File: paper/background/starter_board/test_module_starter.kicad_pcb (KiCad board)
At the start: 2 copper layers, 140.6 x 82 mm, 15 parts, among them J1 Barrel_Jack_12V, J2 RS232_2CH_Module, M1 ERM_Motor, M2 Stepper_4wire, M3 Servo_3pin, U1 D24V22F5_Buck, U2 Pi_Pico_W, U3 DRV2605L_Breakout, U4 DRV8871_Breakout, U5 Tic_T500

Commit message: Align starter-board KiCad trios with PR #100 scale integration (U6 RS-232 on +3V3, SCALE_TX/RX)
Regenerates both upload trios from PR #100's rev B netlist: the Waveshare
Pico-2CH-RS232 becomes U6 reached via its channel-0 4-pin TTL header
(VCC on +3V3 so the TTL swing stays inside the RP2040 abs max), wired
straight across on UART0 (GP12->TXD = SCALE_TX, GP13<-RXD = SCALE_RX);
the 40-pad J2 receptacle model and the spare GP8/GP9 channel nets are
dropped. Board is now 15 footprints / 101 pads / 75 net-assigned /
22 nets. Verified: kicad-cli netlist (75 pins, 22 nets, zero
unconnected), pcbnew DRC (0 courtyard/clearance errors, both trios),
15<->15 footprint<->symbol UUID bijection, byte-for-byte reproducible,
netlist cross-checked ref-by-ref against PR #100's PLACEMENTS
(identical 22-net set), and PR #100's ngspice RS-232 interface
analysis re-run (9/9 PASS).

Co-authored-by: Luke Blaine Winters <288785662+lbwinters@users.noreply.github.com>
Co-Authored-By: Claude Fable 5 <noreply@anthropic.com>
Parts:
- removed J2: RS232_2CH_Module, powder_doser_parts:RS232_2CH_Module
- added U6: Waveshare_2CH_RS232, powder_doser_parts:Waveshare_2CH_RS232, F.Cu at (112.9, 45.5)
- moved M3 0.48 mm to (127.8, 45.5)
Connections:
- U2 pad 11: RS232_1_TXD -> (no net)
- U2 pad 12: RS232_1_RXD -> (no net)
- U2 pad 16: RS232_0_TXD -> SCALE_TX
- U2 pad 17: RS232_0_RXD -> SCALE_RX
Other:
- board size 140.6 x 82 mm -> 140.1 x 82 mm

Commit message: Fix U6 RS-232 module footprint: restore 2x20 receptacle (mid-body 4-pin header was unpluggable)
@lbwinters caught that the generated layout placed the Waveshare
Pico-2CH-RS232 module's pin holes in the middle of its 21x52 mm body,
which would make the physical module impossible to plug in. The PR #100
alignment had adopted that PR's bench-symbol abstraction ("only its
4-pin TTL header reaches the Pico") literally, but the module's own
schematic (hardware/vendor-files/waveshare-pico-2ch-rs232) shows no
such header exists: its TTL signals live only on its 2x20
Pico-form-factor header.

U6 is again the 2x20 side receptacle the module actually plugs onto
(two real PinHeader_1x20 columns at the Pico's 17.78 mm row spacing,
as the pre-PR#100 J2 was), keeping PR #100's electrical intent:
channel 0 straight across to UART0 by board copper (GP12 -> TXD0 =
SCALE_TX, GP13 <- RXD0 = SCALE_RX), VCC (VSYS position) and the
3V3-position LED rail on +3V3, all 8 GND positions grounded,
channel 1 spare.

Board becomes 15 footprints / 137 pads / 83 net-assigned / 22 nets.
Verified: kicad-cli sch export netlist (83 pins, 22 nets, zero
unconnected, both trios), pcbnew 7.0.11 DRC (0 courtyard/clearance
errors), 15<->15 footprint<->symbol UUID bijection, byte-for-byte
reproducible, KiCad 7 20221018 format kept. Both trios + previews
regenerated; note 21, background README, and the vendor-files README
updated.

Co-authored-by: Luke Blaine Winters <288785662+lbwinters@users.noreply.github.com>
Co-Authored-By: Claude Fable 5 <noreply@anthropic.com>
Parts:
- moved M3 0.48 mm to (128.2, 45.5)
- moved U6 0.24 mm to (113.1, 45.5)
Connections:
- U6 pad 1: +3V3 -> SCALE_TX
- U6 pad 2: GND -> SCALE_RX
- U6 pad 3: SCALE_TX -> GND
- U6 pad 4: SCALE_RX -> (no net)
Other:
- board size 140.1 x 82 mm -> 140.6 x 82 mm
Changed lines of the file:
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@@
   )
   (footprint "Connector_PinHeader_2.54mm:PinHeader_1x03_P2.54mm_Vertical" (version 20221018) (generator kiutils) (layer "F.Cu")
-    (at 127.75999999999999 45.510000000000005 0)
+    (at 128.24 45.510000000000005 0)
     (descr "Powder-doser starter-board part; real land pattern(s): Connector_PinHeader_2.54mm:PinHeader_1x03_P2.54mm_Vertical")
     (attr through_hole)
@@
   )
   (footprint "powder_doser_parts:Waveshare_2CH_RS232" (version 20221018) (generator kiutils) (layer "F.Cu")
-    (at 112.91 45.510000000000005 0)
-    (descr "Powder-doser starter-board part; real land pattern(s): Connector_PinHeader_2.54mm:PinHeader_1x04_P2.54mm_Vertical")
+    (at 113.14999999999999 45.510000000000005 0)
+    (descr "Powder-doser starter-board part; real land pattern(s): Connector_PinHeader_2.54mm:PinHeader_1x20_P2.54mm_Vertical")
     (attr through_hole)
     (fp_text reference "U6" (at 0 -27.0 0) (layer "F.SilkS")
@@
       (effects (font (size 1.0 1.0) (thickness 0.15)))
     )
-    (fp_line (start -10.5 -26.0) (end 10.5 -26.0) (layer "F.Fab") (width 0.1))
-    (fp_line (start 10.5 -26.0) (end 10.5 26.0) (layer "F.Fab") (width 0.1))
-    (fp_line (start 10.5 26.0) (end -10.5 26.0) (layer "F.Fab") (width 0.1))
-    (fp_line (start -10.5 26.0) (end -10.5 -26.0) (layer "F.Fab") (width 0.1))
-    (fp_line (start -10.6 -26.1) (end 10.6 -26.1) (layer "F.SilkS") (width 0.12))
-    (fp_line (start 10.6 -26.1) (end 10.6 26.1) (layer "F.SilkS") (width 0.12))
-    (fp_line (start 10.6 26.1) (end -10.6 26.1) (layer "F.SilkS") (width 0.12))
-    (fp_line (start -10.6 26.1) (end -10.6 -26.1) (layer "F.SilkS") (width 0.12))
-    (fp_line (start -11.0 -26.5) (end 11.0 -26.5) (layer "F.CrtYd") (width 0.05))
-    (fp_line (start 11.0 -26.5) (end 11.0 26.5) (layer "F.CrtYd") (width 0.05))
-    (fp_line (start 11.0 26.5) (end -11.0 26.5) (layer "F.CrtYd") (width 0.05))
-    (fp_line (start -11.0 26.5) (end -11.0 -26.5) (layer "F.CrtYd") (width 0.05))
-    (pad "1" thru_hole rect (at 0.0 -3.81 0) (size 1.7 1.7) (drill 1) (layers *.Cu *.Mask)
+    (fp_line (start -10.74 -26.0) (end 10.74 -26.0) (layer "F.Fab") (width 0.1))
+    (fp_line (start 10.74 -26.0) (end 10.74 26.0) (layer "F.Fab") (width 0.1))
+    (fp_line (start 10.74 26.0) (end -10.74 26.0) (layer "F.Fab") (width 0.1))
+    (fp_line (start -10.74 26.0) (end -10.74 -26.0) (layer "F.Fab") (width 0.1))
+    (fp_line (start -10.84 -26.1) (end 10.84 -26.1) (layer "F.SilkS") (width 0.12))
+    (fp_line (start 10.84 -26.1) (end 10.84 26.1) (layer "F.SilkS") (width 0.12))
+    (fp_line (start 10.84 26.1) (end -10.84 26.1) (layer "F.SilkS") (width 0.12))
+    (fp_line (start -10.84 26.1) (end -10.84 -26.1) (layer "F.SilkS") (width 0.12))
+    (fp_line (start -11.24 -26.5) (end 11.24 -26.5) (layer "F.CrtYd") (width 0.05))
+    (fp_line (start 11.24 -26.5) (end 11.24 26.5) (layer "F.CrtYd") (width 0.05))
+    (fp_line (start 11.24 26.5) (end -11.24 26.5) (layer "F.CrtYd") (width 0.05))
+    (fp_line (start -11.24 26.5) (end -11.24 -26.5) (layer "F.CrtYd") (width 0.05))
+    (pad "1" thru_hole rect (at -8.89 -24.13 0) (size 1.7 1.7) (drill 1) (layers *.Cu *.Mask)
+      (net 9 "SCALE_TX") (pinfunction "TXD0"))
+    (pad "2" thru_hole oval (at -8.89 -21.59 0) (size 1.7 1.7) (drill 1) (layers *.Cu *.Mask)
+      (net 8 "SCALE_RX") (pinfunction "RXD0"))
+    (pad "3" thru_hole oval (at -8.89 -19.05 0) (size 1.7 1.7) (drill 1) (layers *.Cu *.Mask)
+      (net 4 "GND") (pinfunction "GND"))
+    (pad "4" thru_hole oval (at -8.89 -16.51 0) (size 1.7 1.7) (drill 1) (layers *.Cu *.Mask)
+      (net 0 "") (pinfunction "GP2"))
+    (pad "5" thru_hole oval (at -8.89 -13.97 0) (size 1.7 1.7) (drill 1) (layers *.Cu *.Mask)
+      (net 0 "") (pinfunction "GP3"))
+    (pad "6" thru_hole oval (at -8.89 -11.43 0) (size 1.7 1.7) (drill 1) (layers *.Cu *.Mask)
+      (net 0 "") (pinfunction "TXD1"))
+    (pad "7" thru_hole oval (at -8.89 -8.89 0) (size 1.7 1.7) (drill 1) (layers *.Cu *.Mask)
+      (net 0 "") (pinfunction "RXD1"))
+    (pad "8" thru_hole oval (at -8.89 -6.35 0) (size 1.7 1.7) (drill 1) (layers *.Cu *.Mask)
+      (net 4 "GND") (pinfunction "GND"))
+    (pad "9" thru_hole oval (at -8.89 -3.81 0) (size 1.7 1.7) (drill 1) (layers *.Cu *.Mask)
+      (net 0 "") (pinfunction "GP6"))
+    (pad "10" thru_hole oval (at -8.89 -1.27 0) (size 1.7 1.7) (drill 1) (layers *.Cu *.Mask)
+      (net 0 "") (pinfunction "GP7"))
+    (pad "11" thru_hole oval (at -8.89 1.27 0) (size 1.7 1.7) (drill 1) (layers *.Cu *.Mask)
+      (net 0 "") (pinfunction "GP8"))
+    (pad "12" thru_hole oval (at -8.89 3.81 0) (size 1.7 1.7) (drill 1) (layers *.Cu *.Mask)
+      (net 0 "") (pinfunction "GP9"))
+    (pad "13" thru_hole oval (at -8.89 6.35 0) (size 1.7 1.7) (drill 1) (layers *.Cu *.Mask)
+      (net 4 "GND") (pinfunction "GND"))
+    (pad "14" thru_hole oval (at -8.89 8.89 0) (size 1.7 1.7) (drill 1) (layers *.Cu *.Mask)
+      (net 0 "") (pinfunction "GP10"))
+    (pad "15" thru_hole oval (at -8.89 11.43 0) (size 1.7 1.7) (drill 1) (layers *.Cu *.Mask)
+      (net 0 "") (pinfunction "GP11"))
+    (pad "16" thru_hole oval (at -8.89 13.97 0) (size 1.7 1.7) (drill 1) (layers *.Cu *.Mask)
+      (net 0 "") (pinfunction "GP12"))
+    (pad "17" thru_hole oval (at -8.89 16.51 0) (size 1.7 1.7) (drill 1) (layers *.Cu *.Mask)
+      (net 0 "") (pinfunction "GP13"))
+    (pad "18" thru_hole oval (at -8.89 19.05 0) (size 1.7 1.7) (drill 1) (layers *.Cu *.Mask)
+      (net 4 "GND") (pinfunction "GND"))
+    (pad "19" thru_hole oval (at -8.89 21.59 0) (size 1.7 1.7) (drill 1) (layers *.Cu *.Mask)
+      (net 0 "") (pinfunction "GP14"))
+    (pad "20" thru_hole oval (at -8.89 24.13 0) (size 1.7 1.7) (drill 1) (layers *.Cu *.Mask)
+      (net 0 "") (pinfunction "GP15"))
+    (pad "21" thru_hole rect (at 8.89 -24.13 0) (size 1.7 1.7) (drill 1) (layers *.Cu *.Mask)
+      (net 0 "") (pinfunction "VBUS"))
+    (pad "22" thru_hole oval (at 8.89 -21.59 0) (size 1.7 1.7) (drill 1) (layers *.Cu *.Mask)
       (net 2 "+3V3") (pinfunction "VCC"))
-    (pad "2" thru_hole oval (at 0.0 -1.27 0) (size 1.7 1.7) (drill 1) (layers *.Cu *.Mask)
+    (pad "23" thru_hole oval (at 8.89 -19.05 0) (size 1.7 1.7) (drill 1) (layers *.Cu *.Mask)
       (net 4 "GND") (pinfunction "GND"))
-    (pad "3" thru_hole oval (at 0.0 1.27 0) (size 1.7 1.7) (drill 1) (layers *.Cu *.Mask)
-      (net 9 "SCALE_TX") (pinfunction "TXD"))
-    (pad "4" thru_hole oval (at 0.0 3.81 0) (size 1.7 1.7) (drill 1) (layers *.Cu *.Mask)
-      (net 8 "SCALE_RX") (pinfunction "RXD"))
+    (pad "24" thru_hole oval (at 8.89 -16.51 0) (size 1.7 1.7) (drill 1) (layers *.Cu *.Mask)
+      (net 0 "") (pinfunction "3V3_EN"))
+    (pad "25" thru_hole oval (at 8.89 -13.97 0) (size 1.7 1.7) (drill 1) (layers *.Cu *.Mask)
+      (net 2 "+3V3") (pinfunction "3V3"))
+    (pad "26" thru_hole oval (at 8.89 -11.43 0) (size 1.7 1.7) (drill 1) (layers *.Cu *.Mask)
+      (net 0 "") (pinfunction "ADC_VREF"))
+    (pad "27" thru_hole oval (at 8.89 -8.89 0) (size 1.7 1.7) (drill 1) (layers *.Cu *.Mask)
+      (net 0 "") (pinfunction "GP28"))
+    (pad "28" thru_hole oval (at 8.89 -6.35 0) (size 1.7 1.7) (drill 1) (layers *.Cu *.Mask)
+      (net 4 "GND") (pinfunction "GND"))
+    (pad "29" thru_hole oval (at 8.89 -3.81 0) (size 1.7 1.7) (drill 1) (layers *.Cu *.Mask)
+      (net 0 "") (pinfunction "GP27"))
+    (pad "30" thru_hole oval (at 8.89 -1.27 0) (size 1.7 1.7) (drill 1) (layers *.Cu *.Mask)
+      (net 0 "") (pinfunction "GP26"))
+    (pad "31" thru_hole oval (at 8.89 1.27 0) (size 1.7 1.7) (drill 1) (layers *.Cu *.Mask)
+      (net 0 "") (pinfunction "RUN"))
+    (pad "32" thru_hole oval (at 8.89 3.81 0) (size 1.7 1.7) (drill 1) (layers *.Cu *.Mask)
+      (net 0 "") (pinfunction "GP22"))
+    (pad "33" thru_hole oval (at 8.89 6.35 0) (size 1.7 1.7) (drill 1) (layers *.Cu *.Mask)
+      (net 4 "GND") (pinfunction "GND"))
+    (pad "34" thru_hole oval (at 8.89 8.89 0) (size 1.7 1.7) (drill 1) (layers *.Cu *.Mask)
+      (net 0 "") (pinfunction "GP21"))
+    (pad "35" thru_hole oval (at 8.89 11.43 0) (size 1.7 1.7) (drill 1) (layers *.Cu *.Mask)
+      (net 0 "") (pinfunction "GP20"))
+    (pad "36" thru_hole oval (at 8.89 13.97 0) (size 1.7 1.7) (drill 1) (layers *.Cu *.Mask)
+      (net 0 "") (pinfunction "GP19"))
+    (pad "37" thru_hole oval (at 8.89 16.51 0) (size 1.7 1.7) (drill 1) (layers *.Cu *.Mask)
+      (net 0 "") (pinfunction "GP18"))
+    (pad "38" thru_hole oval (at 8.89 19.05 0) (size 1.7 1.7) (drill 1) (layers *.Cu *.Mask)
+      (net 4 "GND") (pinfunction "GND"))
+    (pad "39" thru_hole oval (at 8.89 21.59 0) (size 1.7 1.7) (drill 1) (layers *.Cu *.Mask)
+      (net 0 "") (pinfunction "GP17"))
+    (pad "40" thru_hole oval (at 8.89 24.13 0) (size 1.7 1.7) (drill 1) (layers *.Cu *.Mask)
+      (net 0 "") (pinfunction "GP16"))
   )
-  (gr_line (start -5.0 -5.0) (end 135.10999999999999 -5.0) (layer "Edge.Cuts") (width 0.1))
-  (gr_line (start 135.10999999999999 -5.0) (end 135.10999999999999 77.01) (layer "Edge.Cuts") (width 0.1))
-  (gr_line (start 135.10999999999999 77.01) (end -5.0 77.01) (layer "Edge.Cuts") (width 0.1))
+  (gr_line (start -5.0 -5.0) (end 135.59 -5.0) (layer "Edge.Cuts") (width 0.1))
+  (gr_line (start 135.59 -5.0) (end 135.59 77.01) (layer "Edge.Cuts") (width 0.1))
+  (gr_line (start 135.59 77.01) (end -5.0 77.01) (layer "Edge.Cuts") (width 0.1))
   (gr_line (start -5.0 77.01) (end -5.0 -5.0) (layer "Edge.Cuts") (width 0.1))
 )

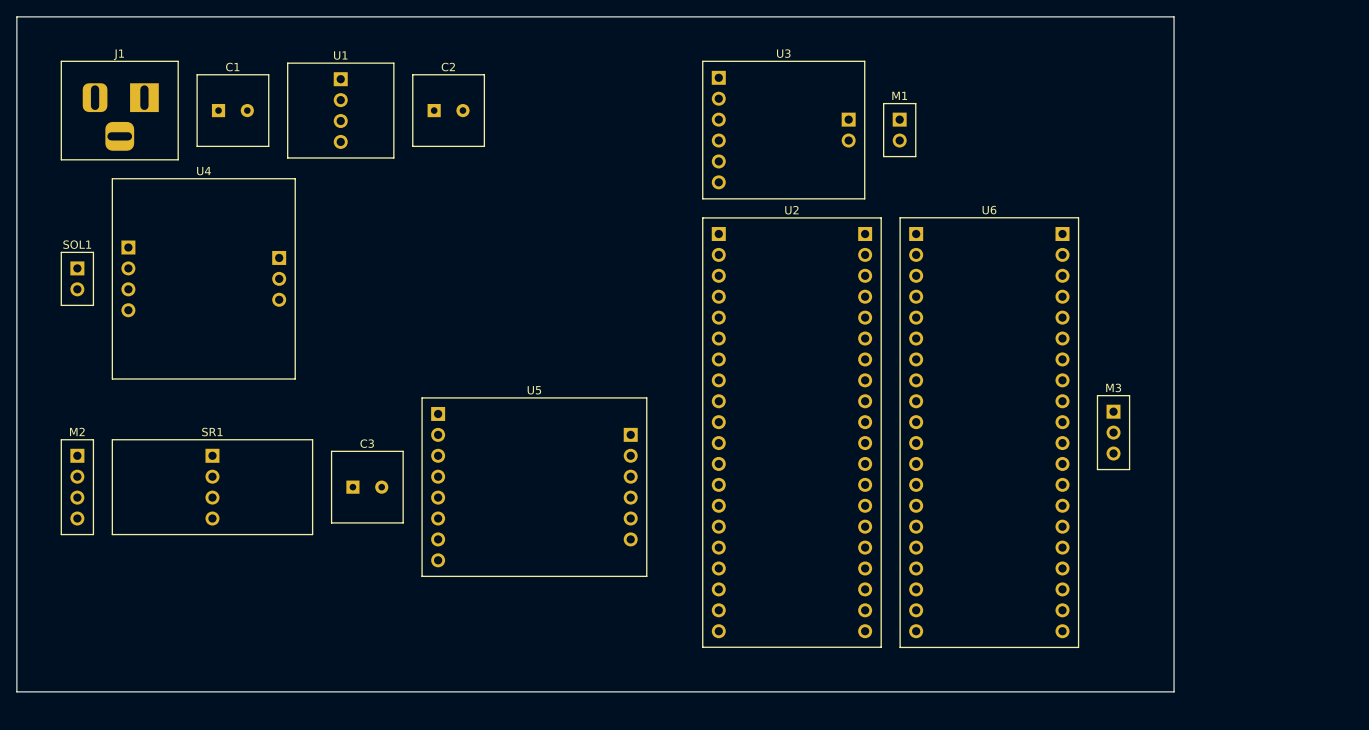
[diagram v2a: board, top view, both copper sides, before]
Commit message: Full physical-footprint audit: vendor-exact hole maps for all 5 carriers + barrel-jack GND fix
Re-verified every component against primary vendor geometry (PR #25 Eagle
.brd files, Pololu reg19a/tvs01a/tic03b dimension diagrams + official
tic03b drill-guide DXF, CUI PJ-102AH datasheet, Waveshare module schematic,
Pico mechanical drawing) per PR #76 review request. Fixes five unpluggable
land patterns (Tic T500 38.1x26.7 mm with all 29 real holes and correct
A2/A1 order; D24V22F5 17.8x17.8 mm PG/EN/VIN/GND/VOUT row + offset GND;
shunt regulator 28.6x20.3 mm wire terminals; DRV8871 3.5 mm terminal
blocks + 1x4 logic header; DRV2605L STEMMA QT 1x5 row with real SCL/SDA
order, EN pin dropped as nonexistent) and one wiring fault (barrel-jack
GND was on the switch lug, which floats when a plug is inserted; now on
the sleeve). Boards grow to 172 pads / 95 net-assigned / 22 nets; the
unplaced auto-place outline is re-sized 100x100 -> 110x110 mm to stay in
the 35-55% utilisation band with the real bodies. kicad-cli netlist
(95 pins, zero unconnected), pcbnew DRC (no courtyard/clearance/short
errors), 15<->15 footprint<->symbol UUID bijection, and byte-for-byte
reproducibility all re-verified on both trios.

Co-authored-by: Luke Blaine Winters <288785662+lbwinters@users.noreply.github.com>
Co-Authored-By: Claude Fable 5 <noreply@anthropic.com>
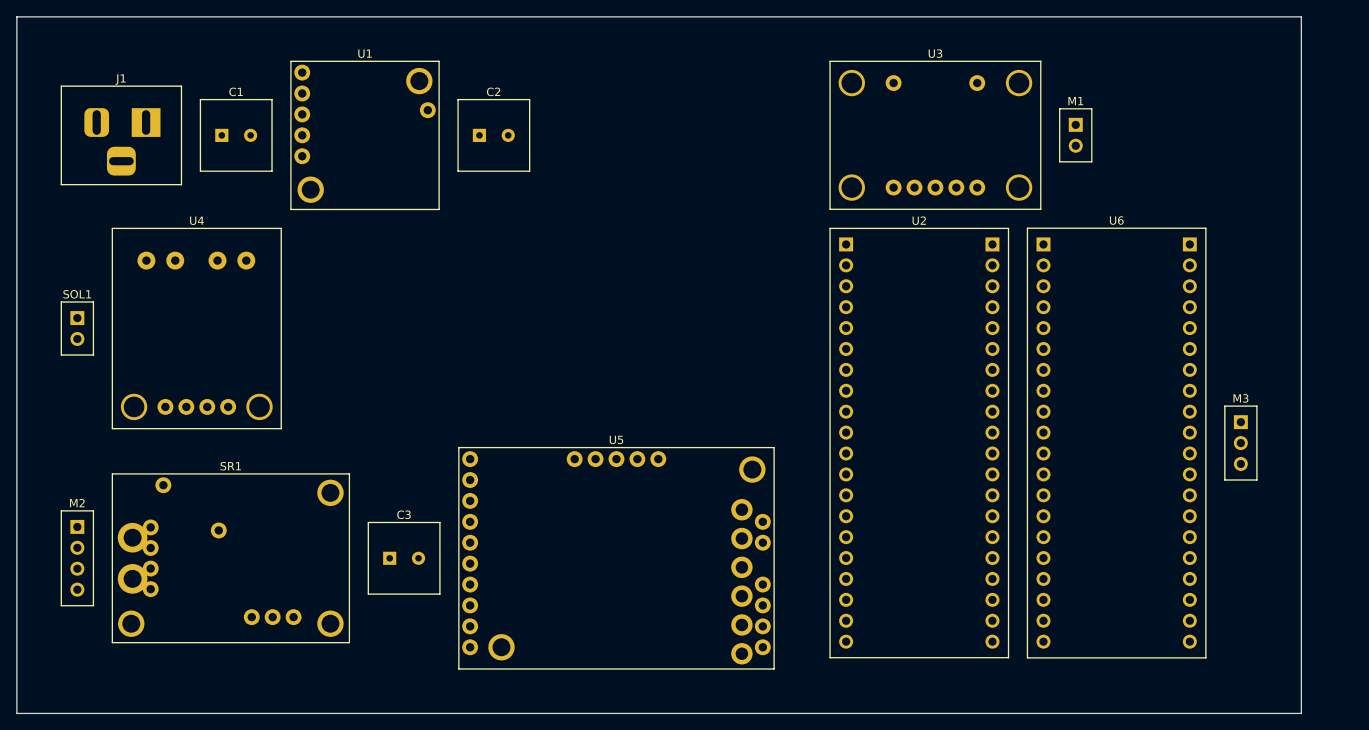
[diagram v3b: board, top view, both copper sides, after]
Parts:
- moved M1 21.4 mm to (123.7, 9.39)
- moved U3 18.4 mm to (106.6, 9.39)
- moved U2 15.5 mm to (104.6, 46.8)
- moved U6 15.5 mm to (128.6, 46.8)
- moved M3 15.5 mm to (143.7, 46.8)
- moved U5 13.2 mm to (67.9, 60.8)
- moved C3 9.73 mm to (42.1, 60.8)
- moved SR1 8.93 mm to (21.0, 60.8)
- moved M2 8.64 mm to (2.35, 60.8)
- moved C2 6.27 mm to (53.0, 9.40)
- moved U4 6.09 mm to (16.9, 32.9)
- moved SOL1 6.03 mm to (2.35, 32.9)
- moved U1 4.22 mm to (37.3, 9.40)
- moved C1 3.04 mm to (21.6, 9.40)
- moved J1 3.02 mm to (7.70, 9.40)
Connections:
- SR1 pad 3: GND -> +12V
- U1 pad 1: +12V -> (no net)
- U1 pad 2: GND -> +12V
- U1 pad 3: +5V -> +12V
- U1 pad 4: +12V -> GND
- U3 pad 3: I2C_SDA -> I2C_SCL
- U3 pad 4: I2C_SCL -> I2C_SDA
- U3 pad 6: HAPT_EN -> VIB_A
- U3 pad 7: VIB_A -> VIB_B
- U3 pad 8: VIB_B -> (no net)
- U4 pad 1: +12V -> SOL_B
- U4 pad 2: GND -> SOL_A
- U4 pad 3: SOL_A -> +12V
- U4 pad 4: SOL_B -> GND
- U4 pad 5: SOL_IN1 -> SOL_IN2
- U4 pad 6: SOL_IN2 -> SOL_IN1
- U4 pad 7: GND -> +12V
- U5 pad 11: STP_A1 -> (no net)
- U5 pad 12: STP_A2 -> (no net)
- U5 pad 13: STP_B1 -> GND
- U5 pad 14: STP_B2 -> GND
- U5 pad 3: STP_RX -> (no net)
- U5 pad 4: STP_TX -> (no net)
- U5 pad 5: (no net) -> GND
- U5 pad 6: (no net) -> STP_RX
- U5 pad 7: GND -> STP_TX
- U5 pad 9: +12V -> (no net)
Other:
- board size 140.6 x 82 mm -> 156.1 x 84.6 mm

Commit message: Add second dispensing-angle servo M4 (SERVO_SIG2 on GP2) — 2-servo design alignment
williamulbz's PR #76 review flagged that the board predates the move to
the 2-servo design (PR #66 dual-servo hinge; PR #100 generate.py rev C).
build_starter_board.py now emits a second 3-pin servo header M4 wired
exactly as rev C: SIG -> SERVO_SIG2 on Pico GP2 (mirrored in firmware via
config.SERVO2_INVERT), +5V/GND shared. M4 joins the logic/mcu placement
cluster beside M3, edge-biased for cable exit.

Counts: 16 footprints / 175 pads / 99 net-assigned / 23 nets (placed
outline ~162x85 mm; unplaced stays 110x110 mm at ~51% courtyard).
Verified: kicad-cli netlist 99 pins / 23 nets / zero unconnected on both
trios (SERVO_SIG2 = M4.3 <-> U2.4/GP2), pcbnew DRC clean (no courtyard/
clearance/short errors), 16<->16 footprint<->symbol UUID bijection,
byte-for-byte reproducible, KiCad 7 20221018 format kept. Both trios +
previews + summary regenerated; note 21 update block, note 24 superseded
caveat (run-2 candidates lack M4; +5V now wants 2000 mA in Quilter), and
background README updated.

Co-authored-by: Sterling G. Baird <45469701+sgbaird@users.noreply.github.com>
Co-Authored-By: Claude Fable 5 <noreply@anthropic.com>
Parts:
- added M4: Servo_3pin, Connector_PinHeader_2.54mm:PinHeader_1x03_P2.54mm_Vertical, F.Cu at (149.9, 46.8)
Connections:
- U2 pad 4: (no net) -> SERVO_SIG2
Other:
- board size 156.1 x 84.6 mm -> 162.3 x 84.6 mm
